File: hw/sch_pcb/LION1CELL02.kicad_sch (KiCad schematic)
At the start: 93 parts, among them J1 USBC_USB4105-GF-A, J2 HEADER_2x03, J3 HEADER_1x04, Q1 BSS83P, Q2 BC807-25, Q3 BC807-25, Q4 AO3400A, Q5 AO3400A, SW1 SKRTLAE010, U1 BQ34Z100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

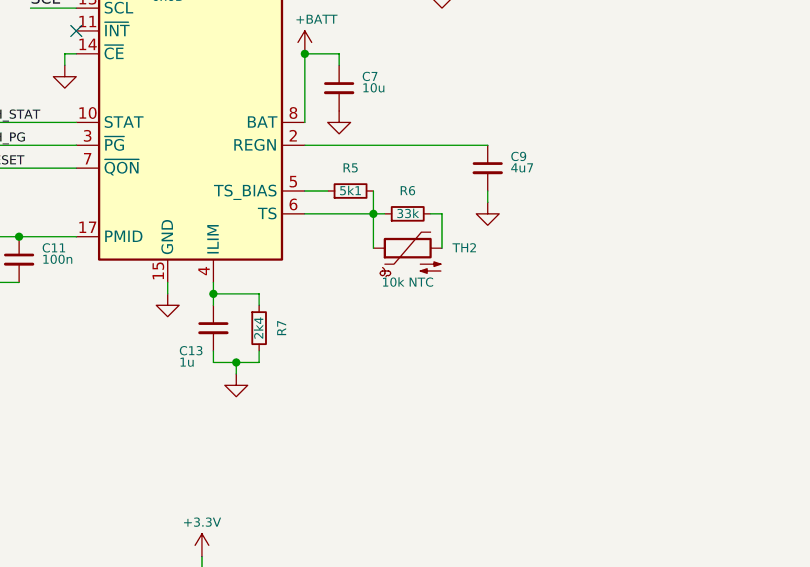
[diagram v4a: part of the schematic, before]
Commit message: Fix termistor unconnection https://github.com/mlab-modules/BATDATUNIT01/issues/16
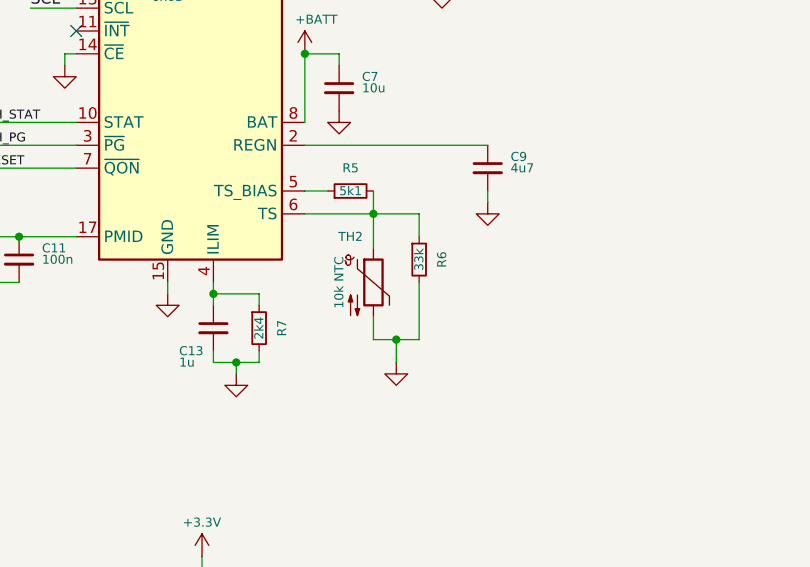
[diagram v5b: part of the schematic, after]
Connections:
- net GND: now also R6.2, TH2.2
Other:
- moved on the sheet: R6, TH2
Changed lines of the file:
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@@
 	)
 	(junction
+		(at 212.09 100.33)
+		(diameter 0)
+		(color 0 0 0 0)
+	)
+	(junction
 		(at 196.85 231.14)
 		(diameter 0)
@@
 	(wire
 		(pts
+			(xy 214.63 93.98) (xy 214.63 100.33)
+		)
+		(stroke
+			(width 0)
+			(type default)
+		)
+	)
+	(wire
+		(pts
 			(xy 191.77 95.25) (xy 191.77 93.98)
 		)
@@
 	(wire
 		(pts
-			(xy 209.55 86.36) (xy 210.82 86.36)
+			(xy 209.55 86.36) (xy 214.63 86.36)
 		)
 		(stroke
@@
 	(wire
 		(pts
+			(xy 209.55 100.33) (xy 212.09 100.33)
+		)
+		(stroke
+			(width 0)
+			(type default)
+		)
+	)
+	(wire
+		(pts
 			(xy 58.42 143.51) (xy 58.42 144.78)
 		)
@@
 	(wire
 		(pts
-			(xy 190.5 124.46) (xy 190.5 125.73)
+			(xy 209.55 97.79) (xy 209.55 100.33)
 		)
 		(stroke
@@
 	(wire
 		(pts
-			(xy 233.68 189.23) (xy 233.68 193.04)
+			(xy 190.5 124.46) (xy 190.5 125.73)
 		)
 		(stroke
@@
 	(wire
 		(pts
-			(xy 93.98 264.16) (xy 96.52 264.16)
+			(xy 233.68 189.23) (xy 233.68 193.04)
 		)
 		(stroke
@@
 	(wire
 		(pts
-			(xy 55.88 143.51) (xy 55.88 144.78)
+			(xy 93.98 264.16) (xy 96.52 264.16)
 		)
 		(stroke
@@
 	(wire
 		(pts
-			(xy 217.17 86.36) (xy 217.17 90.17)
+			(xy 55.88 143.51) (xy 55.88 144.78)
 		)
 		(stroke
@@
 	(wire
 		(pts
+			(xy 212.09 100.33) (xy 212.09 102.87)
+		)
+		(stroke
+			(width 0)
+			(type default)
+		)
+	)
+	(wire
+		(pts
 			(xy 342.9 153.67) (xy 342.9 154.94)
 		)
@@
 	(wire
 		(pts
+			(xy 214.63 86.36) (xy 214.63 88.9)
+		)
+		(stroke
+			(width 0)
+			(type default)
+		)
+	)
+	(wire
+		(pts
 			(xy 44.45 269.24) (xy 45.72 269.24)
 		)
@@
 	(wire
 		(pts
-			(xy 215.9 86.36) (xy 217.17 86.36)
-		)
-		(stroke
-			(width 0)
-			(type default)
-		)
-	)
-	(wire
-		(pts
 			(xy 191.77 102.87) (xy 191.77 101.6)
 		)
@@
 	(wire
 		(pts
+			(xy 214.63 100.33) (xy 212.09 100.33)
+		)
+		(stroke
+			(width 0)
+			(type default)
+		)
+	)
+	(wire
+		(pts
 			(xy 346.71 91.44) (xy 346.71 90.17)
 		)
@@
 	)
 	(symbol
+		(lib_id "power:GND")
+		(at 212.09 102.87 0)
+		(unit 1)
+		(body_style 1)
+		(exclude_from_sim no)
+		(in_bom yes)
+		(on_board yes)
+		(in_pos_files yes)
+		(dnp no)
+		(property "Reference" "#PWR055"
+			(at 212.09 109.22 0)
+			(hide yes)
+			(show_name no)
+			(do_not_autoplace no)
+			(effects
+				(font
+					(size 1 1)
+				)
+			)
+		)
+		(property "Value" "GND"
+			(at 214.63 102.87 0)
+			(hide yes)
+			(show_name no)
+			(do_not_autoplace no)
+			(effects
+				(font
+					(size 1 1)
+				)
+			)
+		)
+		(property "Footprint" ""
+			(at 212.09 102.87 0)
+			(hide yes)
+			(show_name no)
+			(do_not_autoplace no)
+			(effects
+				(font
+					(size 1 1)
+				)
+			)
+		)
+		(property "Datasheet" ""
+			(at 212.09 102.87 0)
+			(hide yes)
+			(show_name no)
+			(do_not_autoplace no)
+			(effects
+				(font
+					(size 1 1)
+				)
+			)
+		)
+		(property "Description" "Power symbol creates a global label with name \"GND\" , ground"
+			(at 212.09 102.87 0)
+			(hide yes)
+			(show_name no)
+			(do_not_autoplace no)
+			(effects
+				(font
+					(size 1.27 1.27)
+				)
+			)
+		)
+		(pin "1"
+		)
+		(instances
+			(project "LION1CELL02"
+				(path "/949a5bba-1f1f-4325-9d02-2c6814a96048"
+					(reference "#PWR055")
+					(unit 1)
+				)
+			)
+		)
+	)
+	(symbol
 		(lib_id "power:+BATT")
 		(at 60.96 266.7 270)
@@
 	(symbol
 		(lib_id "Device:Thermistor_NTC")
-		(at 213.36 90.17 90)
+		(at 209.55 93.98 0)
 		(unit 1)
 		(body_style 1)
@@
 		(dnp no)
 		(property "Reference" "TH2"
-			(at 219.71 90.17 90)
+			(at 207.01 88.9 0)
 			(show_name no)
 			(do_not_autoplace no)
@@
 		)
 		(property "Value" "10k NTC"
-			(at 213.36 93.98 90)
+			(at 205.74 93.98 90)
 			(show_name no)
 			(do_not_autoplace no)
@@
 		)
 		(property "Footprint" "Resistor_SMD:R_0805_2012Metric"
-			(at 212.09 90.17 0)
+			(at 209.55 92.71 0)
 			(hide yes)
 			(show_name no)
@@
 		)
 		(property "Datasheet" ""
-			(at 212.09 90.17 0)
+			(at 209.55 92.71 0)
 			(hide yes)
 			(show_name no)
@@
 		)
 		(property "Description" "Temperature dependent resistor, negative temperature coefficient"
-			(at 213.36 90.17 0)
+			(at 209.55 93.98 0)
 			(hide yes)
 			(show_name no)
@@
 		)
 		(property "UST_ID" "5c70984712875079b91f8ac5"
-			(at 213.36 90.17 0)
+			(at 209.55 93.98 0)
 			(hide yes)
 			(show_name no)
@@
 	(symbol
 		(lib_id "Device:R_Small")
-		(at 213.36 86.36 90)
+		(at 214.63 91.44 0)
 		(unit 1)
 		(body_style 1)
@@
 		(dnp no)
 		(property "Reference" "R6"
-			(at 213.36 83.82 90)
+			(at 217.17 91.44 90)
 			(show_name no)
 			(do_not_autoplace no)
@@
 		)
 		(property "Value" "33k"
-			(at 213.36 86.36 90)
+			(at 214.63 91.44 90)
 			(show_name no)
 			(do_not_autoplace no)
@@
 		)
 		(property "Footprint" "Resistor_SMD:R_0805_2012Metric"
-			(at 213.36 86.36 0)
+			(at 214.63 91.44 0)
 			(hide yes)
 			(show_name no)
@@
 		)
 		(property "Datasheet" ""
-			(at 213.36 86.36 0)
+			(at 214.63 91.44 0)
 			(hide yes)
 			(show_name no)
@@
 		)
 		(property "Description" "Resistor, small symbol"
-			(at 213.36 86.36 0)
+			(at 214.63 91.44 0)
 			(hide yes)
 			(show_name no)
@@
 		)
 		(property "UST_ID" "5c70984712875079b91f8a8a"
-			(at 213.36 86.36 0)
+			(at 214.63 91.44 0)
 			(hide yes)
 			(show_name no)
